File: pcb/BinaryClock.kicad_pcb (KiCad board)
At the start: 2 copper layers, 15 parts, among them CON1 AVR-ISP-6, IC1 ATMEGA328P-A, U1 LM78M05CT, U3 clock_header, U4 clock_header, U5 clock_header, Y1 16MHz

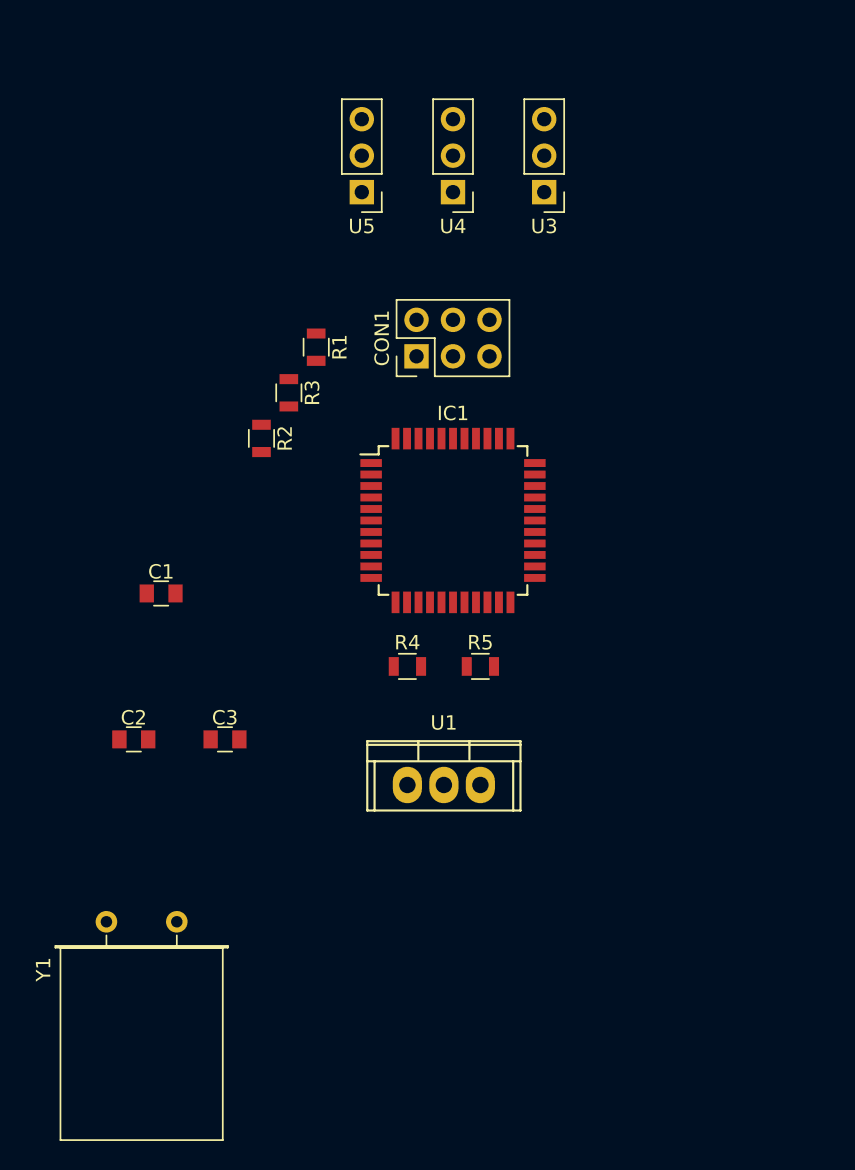
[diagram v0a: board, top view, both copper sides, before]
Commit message: Progress toward high level board layout. Board is still missing a voltage reulator
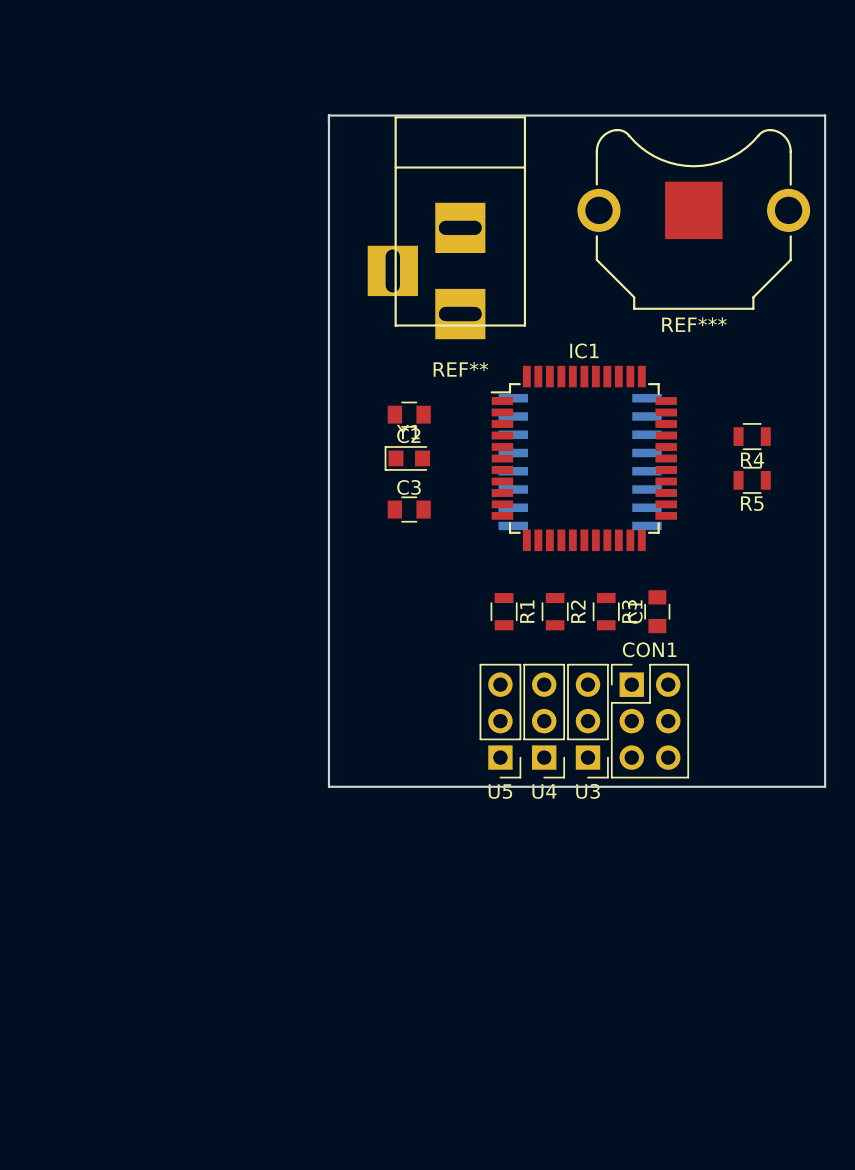
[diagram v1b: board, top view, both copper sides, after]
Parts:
- removed U1: LM78M05CT, Power_Integrations:TO-220
- added ?: , tapMatrix_Shield:DS3231, B.Cu at (159.0, 81.3)
- added REF**: BARREL_JACK, Connectors:BARREL_JACK, F.Cu at (150.4, 64.5)
- added REF***: Keystone_3001_1x12mm-CoinCell, Battery_Holders:Keystone_3001_1x12mm-CoinCell, F.Cu at (166.6, 63.5)
- Y1: footprint Crystals:Crystal_HC18-U_Horizontal -> Crystals:Crystal_SMD_2012-2pin_2.0x1.2mm_HandSoldering
- moved U5 40.5 mm to (153.2, 101.6)
- moved U4 39.9 mm to (156.2, 101.6)
- moved U3 39.5 mm to (159.3, 101.6)
- moved Y1 38.5 mm to (146.8, 80.8)
- moved C1 34.6 mm to (164.1, 91.4), turned to 90 degrees
- moved C2 29.6 mm to (146.8, 77.7), turned to 180 degrees
- moved R4 28.8 mm to (170.7, 79.2), turned to 180 degrees
- moved CON1 27.3 mm to (162.3, 96.5), turned to 0 degrees
- moved R3 26.8 mm to (160.5, 91.4)
- moved R2 23.7 mm to (157.0, 91.4)
- moved R5 22.9 mm to (170.7, 82.3), turned to 180 degrees
- moved R1 22.6 mm to (153.4, 91.4)
- moved C3 20.5 mm to (146.8, 84.3)
- moved IC1 10.1 mm to (159.0, 80.8)
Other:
- board outline added: 34.5 x 46.7 mm

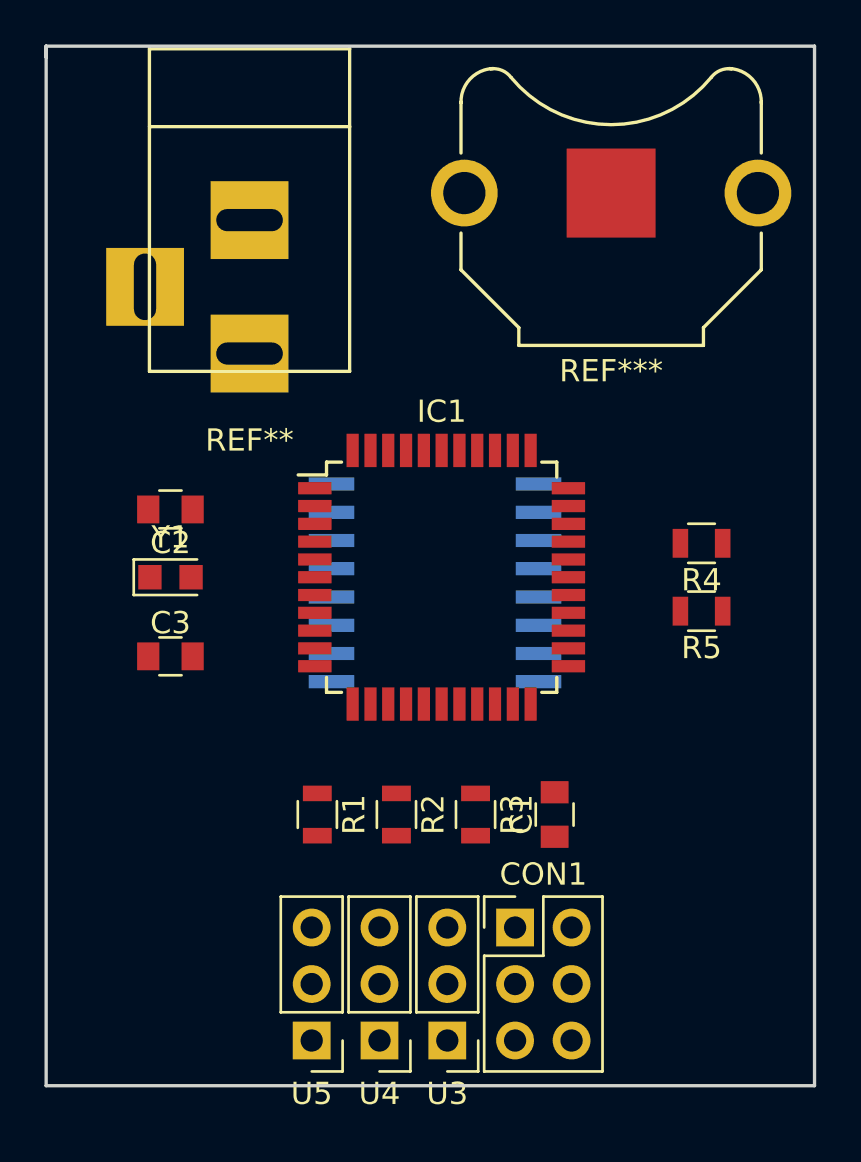
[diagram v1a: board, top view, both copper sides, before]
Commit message: Added voltage regulator to pcb schematic and layout. Started routing on the board layout
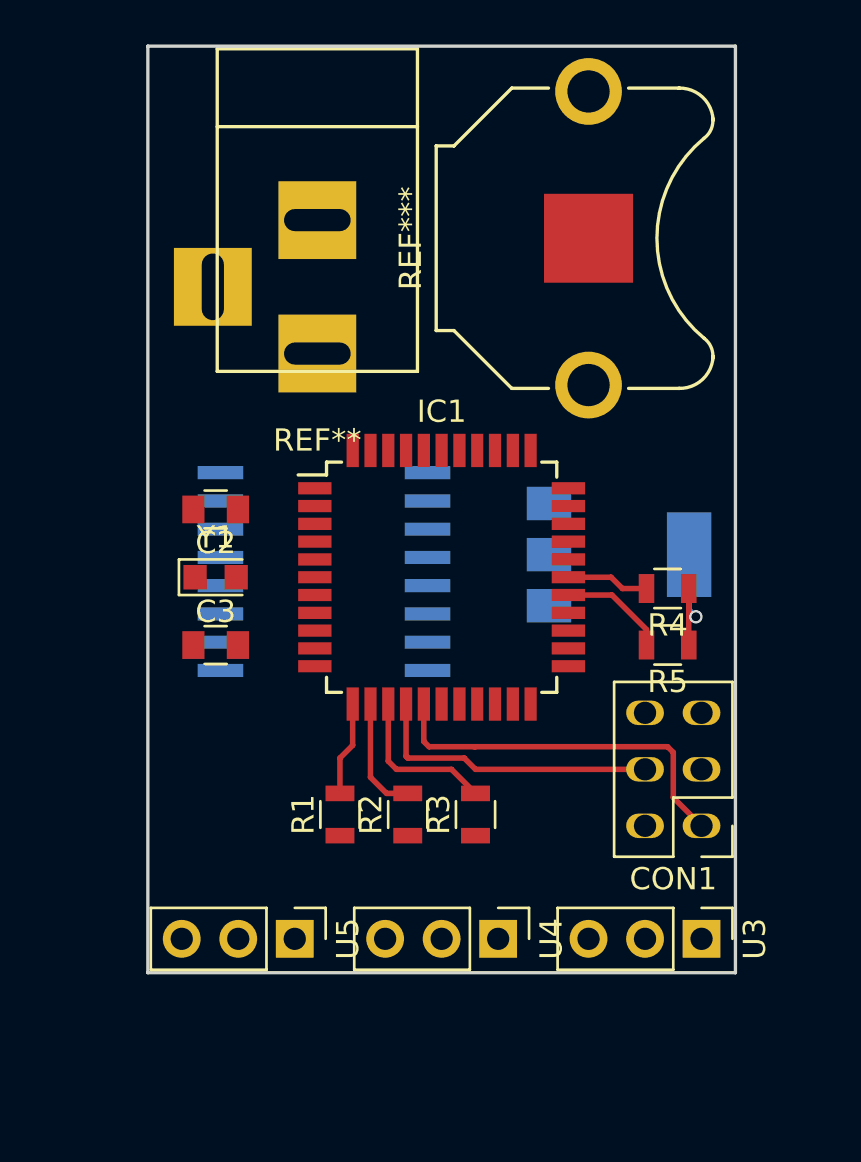
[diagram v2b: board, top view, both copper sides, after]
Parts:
- removed C1: C, Capacitors_SMD:C_0805
- added U1: MC33269, tapMatrix_Shield:SOT223_318H, B.Cu at (163.8, 79.8)
- moved U3 12.3 mm to (170.7, 97.0), turned to 270 degrees
- moved CON1 9.55 mm to (170.7, 91.9), turned to 180 degrees
- moved U4 7.03 mm to (161.5, 97.0), turned to 270 degrees
- moved ? 5.68 mm to (153.4, 80.3), turned to 270 degrees
- moved U5 4.64 mm to (152.4, 97.0), turned to 270 degrees
- moved REF** 3.05 mm to (153.4, 64.5)
- moved R4 2.54 mm to (169.2, 81.3)
- moved REF*** 2.27 mm to (165.6, 65.5), turned to 90 degrees
- moved R5 2.16 mm to (169.2, 83.8)
- moved C3 2.09 mm to (148.8, 83.8)
- moved C2 2.03 mm to (148.8, 77.7)
- moved Y1 2.03 mm to (148.8, 80.8)
- moved R1 1.02 mm to (154.4, 91.4), turned to 90 degrees
- moved R2 0.51 mm to (157.5, 91.4), turned to 90 degrees
- turned R3 to 90 degrees
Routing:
- net /MISO: track 0.00 -> 16.9 mm
- net /MOSI: track 0.00 -> 13.3 mm
- net Net-(IC1-Pad14): track 0.00 -> 7.09 mm
- net VCC: track 0.00 -> 5.78 mm, vias 0 -> 1
- net Net-(IC1-Pad13): track 0.00 -> 5.27 mm
- net SDA: track 0.00 -> 4.85 mm
- net Net-(IC1-Pad12): track 0.00 -> 4.25 mm
- net SCL: track 0.00 -> 3.72 mm
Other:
- board size 34.5 x 46.7 mm -> 26.4 x 41.7 mm

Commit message: Finished initial attempt at routing
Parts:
- removed ?: , tapMatrix_Shield:DS3231
- removed REF**: BARREL_JACK, Connectors:BARREL_JACK
- removed REF***: Keystone_3001_1x12mm-CoinCell, Battery_Holders:Keystone_3001_1x12mm-CoinCell
- added BT1: Battery_Cell, Battery_Holders:Keystone_3001_1x12mm-CoinCell, F.Cu at (165.6, 65.5)
- added CON2: BARREL_JACK, Connectors:BARREL_JACK, F.Cu at (153.2, 64.5)
- added U2: DS3231, tapMatrix_Shield:DS3231, B.Cu at (153.4, 80.5)
- moved U3 18.3 mm to (152.4, 97.0)
- moved U5 18.3 mm to (170.7, 97.0)
- turned C2 to 0 degrees
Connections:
- IC1 pad 18: Net-(IC1-Pad18) -> VCC
- U3 pad 1: (no net) -> GND
- U3 pad 2: (no net) -> /VIN
- U3 pad 3: (no net) -> /LED1
- U4 pad 1: (no net) -> GND
- U4 pad 2: (no net) -> /VIN
- U4 pad 3: (no net) -> /LED2
- U5 pad 1: (no net) -> GND
- U5 pad 2: (no net) -> /VIN
- U5 pad 3: (no net) -> /LED3
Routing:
- net /VIN: track 0.00 -> 87.9 mm
- net VCC: track 5.78 -> 67.5 mm, vias 1 -> 3
- net SDA: track 4.85 -> 21.3 mm, vias 0 -> 1
- net Net-(BT1-Pad1): track 0.00 -> 14.2 mm
- net /SCK: track 0.00 -> 14.0 mm
- net /RESET: track 0.00 -> 13.8 mm
- net SCL: track 3.72 -> 15.9 mm, vias 0 -> 1
- net Net-(C2-Pad2): track 0.00 -> 9.78 mm
- net /LED1: track 0.00 -> 9.52 mm
- net /LED3: track 0.00 -> 7.49 mm
- net Net-(C3-Pad2): track 0.00 -> 7.14 mm
- net /LED2: track 0.00 -> 5.06 mm
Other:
- net class wide added: clearance 0.2, trace_width 3, via_dia 0.6, via_drill 0.4

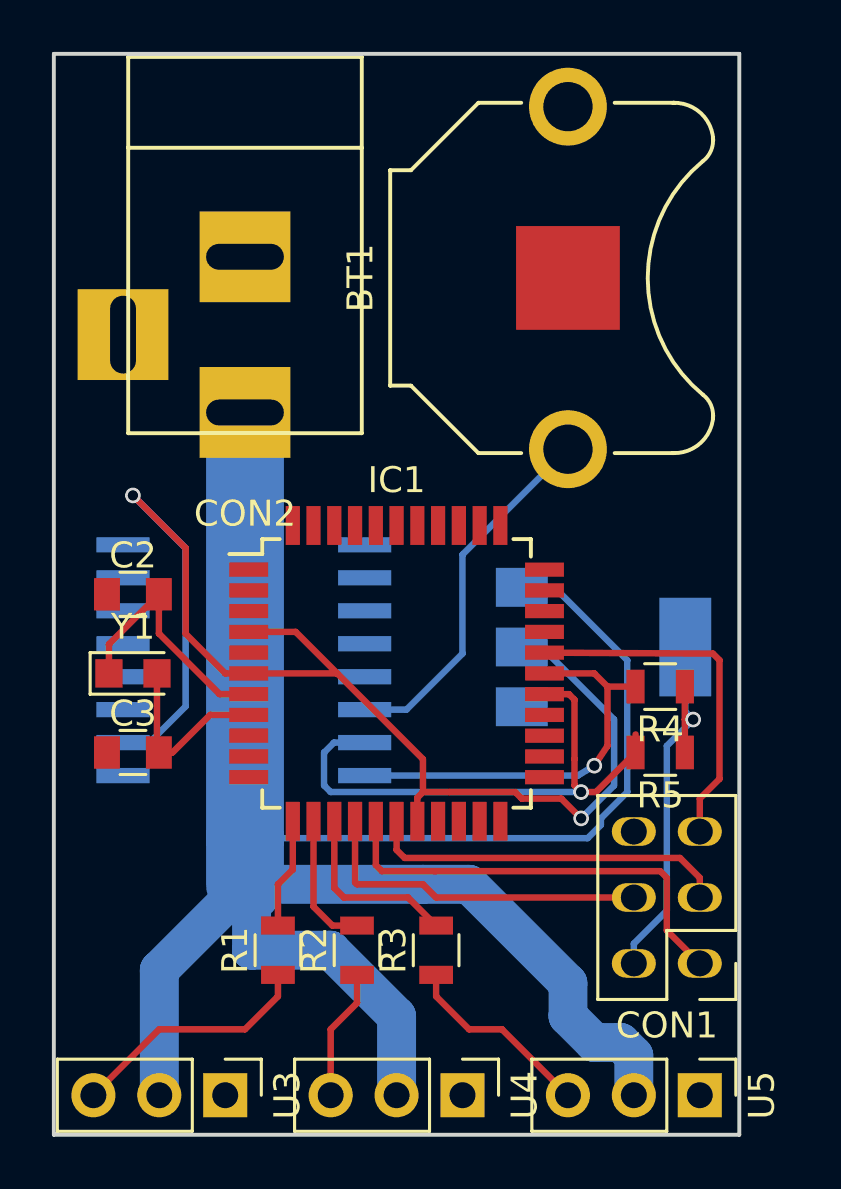
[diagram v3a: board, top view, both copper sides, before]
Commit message: Ground planes added
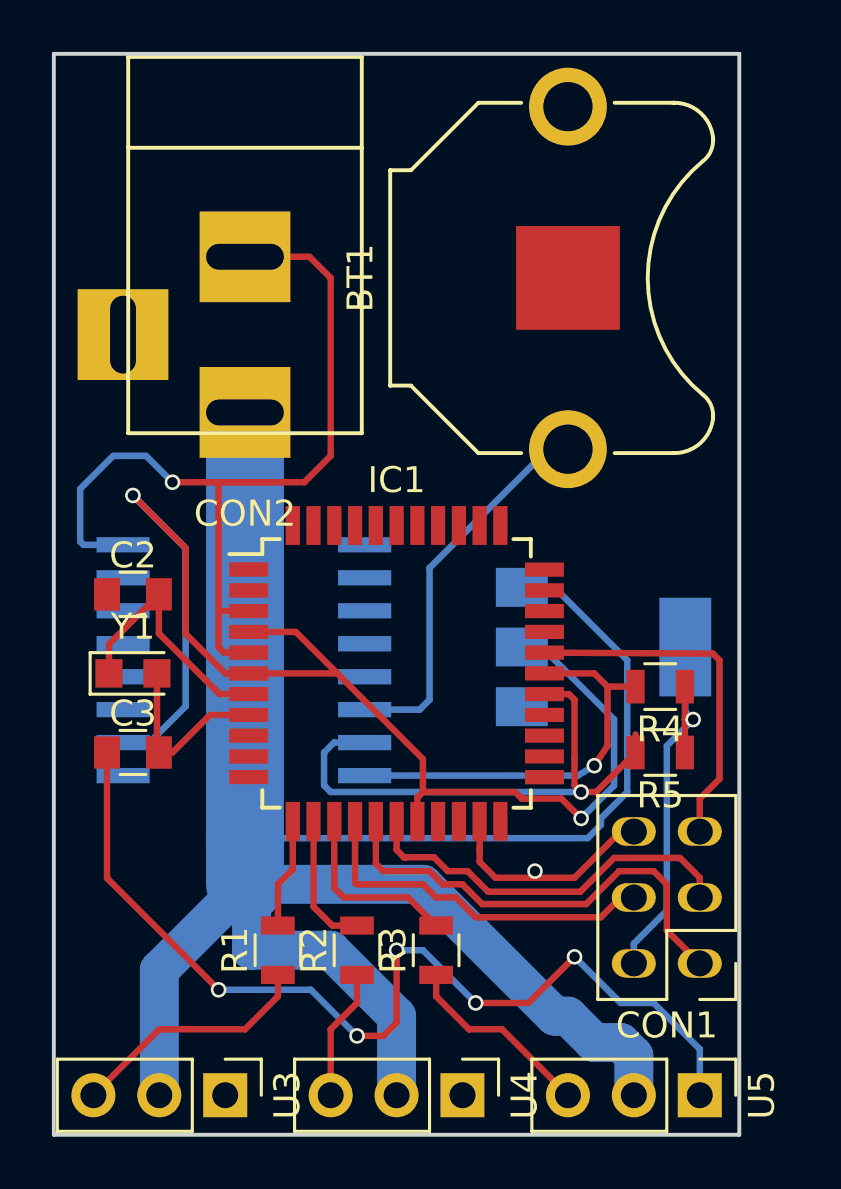
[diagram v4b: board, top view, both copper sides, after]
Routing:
- net GND: track 0.00 -> 80.7 mm, vias 0 -> 7
- net /SCK: track 14.0 -> 15.1 mm
- net /MISO: track 16.9 -> 17.8 mm
- net /VIN: track 87.9 -> 87.1 mm
- net Net-(BT1-Pad1): track 14.2 -> 15.0 mm
- net /MOSI: track 13.3 -> 14.0 mm
- added copper zone on B.Cu, net GND
- added copper zone on F.Cu, net GND

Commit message: Moved left edge of the board layout to increase surface area for the ground plane
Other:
- board size 26.4 x 41.7 mm -> 28.4 x 41.7 mm
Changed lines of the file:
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@@
-(kicad_pcb (version 4) (host pcbnew 4.0.5-e0-6337~49~ubuntu16.04.1)
+(kicad_pcb (version 4) (host pcbnew 4.0.5)
   (general
     (links 52)
     (no_connects 2)
-    (area 145.720999 56.820999 172.287001 98.627001)
+    (area 143.955 56.651519 174.983001 102.108953)
     (thickness 1.6)
-    (drawings 4)
+    (drawings 6)
     (tracks 207)
     (zones 0)
@@
       (net 11 SCL))
   )
+  (gr_line (start 143.764 98.552) (end 145.796 98.552) (angle 90) (layer Edge.Cuts) (width 0.15))
+  (gr_line (start 143.764 56.896) (end 143.764 98.552) (angle 90) (layer Edge.Cuts) (width 0.15))
+  (gr_line (start 145.796 56.896) (end 143.764 56.896) (angle 90) (layer Edge.Cuts) (width 0.15))
   (gr_line (start 145.796 98.552) (end 172.212 98.552) (angle 90) (layer Edge.Cuts) (width 0.15))
   (gr_line (start 172.212 56.896) (end 145.796 56.896) (angle 90) (layer Edge.Cuts) (width 0.15))
   (gr_line (start 172.212 98.552) (end 172.212 56.896) (angle 90) (layer Edge.Cuts) (width 0.15))
-  (gr_line (start 145.796 98.552) (end 145.796 56.896) (angle 90) (layer Edge.Cuts) (width 0.15))
   (segment (start 152.146 78.372) (end 152.146 79.248) (width 0.25) (layer F.Cu) (net 1))
   (segment (start 152.362 79.972) (end 153.304 79.972) (width 0.25) (layer F.Cu) (net 1))
@@
     (polygon
       (pts
-        (xy 172.212 98.552) (xy 145.796 98.552) (xy 145.796 56.896) (xy 172.212 56.896)
+        (xy 143.764 98.552) (xy 143.764 56.896) (xy 172.212 56.896) (xy 172.212 98.552) (xy 145.796 98.552)
+      )
+    )
+    (polygon
+      (pts        (xy 145.796 98.298) (xy 145.785159 98.298) (xy 145.796 98.552)
       )
     )
@@
     (polygon
       (pts
-        (xy 172.212 98.552) (xy 145.796 98.552) (xy 145.796 56.896) (xy 172.212 56.896)
+        (xy 172.212 98.552) (xy 143.764 98.552) (xy 143.764 56.896) (xy 172.212 56.896)
       )
     )
